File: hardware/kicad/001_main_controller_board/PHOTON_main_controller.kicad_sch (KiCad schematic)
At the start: 88 parts, among them J1 FH34SRJ-18S-0.5SH(50), J102 JST_SH RS-485_1, J103 JST_SH RS-485_2, J3 USB_C_Receptacle_USB2.0, J4 Micro_SD_Card, J6 Conn_01x04, SW1 SW_Push, U1 RP2350_60QFN, U101 APS6404L-3SQR-ZR, U102 THVD1424RGTR, U2 NCP1117-3.3_SOT223, U3 W25Q128JVPIQ, U4 TPD4E05U06DQAR, Y1 ABM8-272-T3

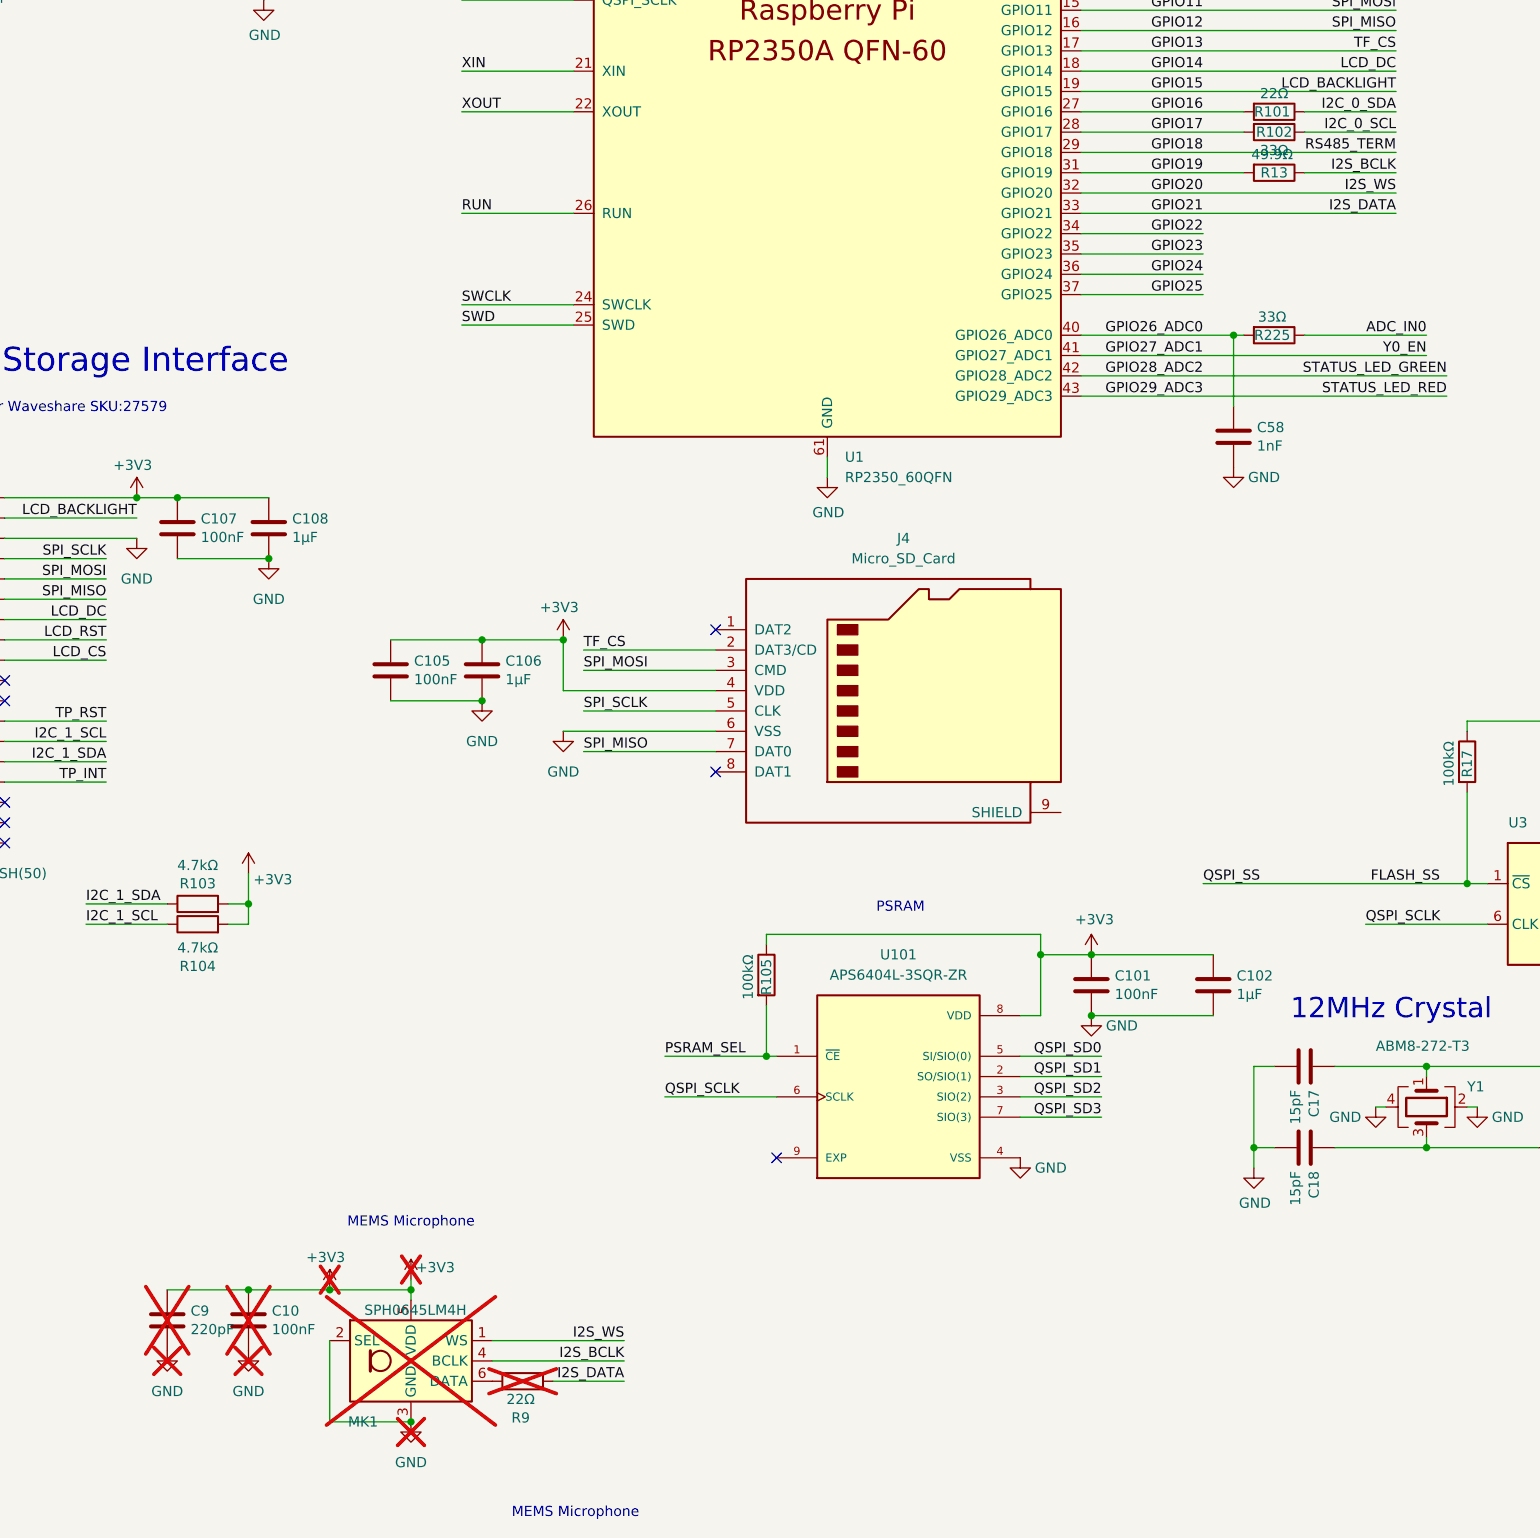
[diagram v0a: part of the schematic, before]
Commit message: Repo hygiene: untrack fab zips and committed .pyc artifacts
The production/*.zip archives are regenerable from the KiCad source, and
the BOM/positions/designators CSVs beside them stay tracked. The .pyc
files predate the __pycache__ ignore rule, so the rule never applied to
them.

Also removes production_rev B.zip, a Finder-created archive carrying
__MACOSX resource forks.

Co-Authored-By: Claude Opus 5 <noreply@anthropic.com>
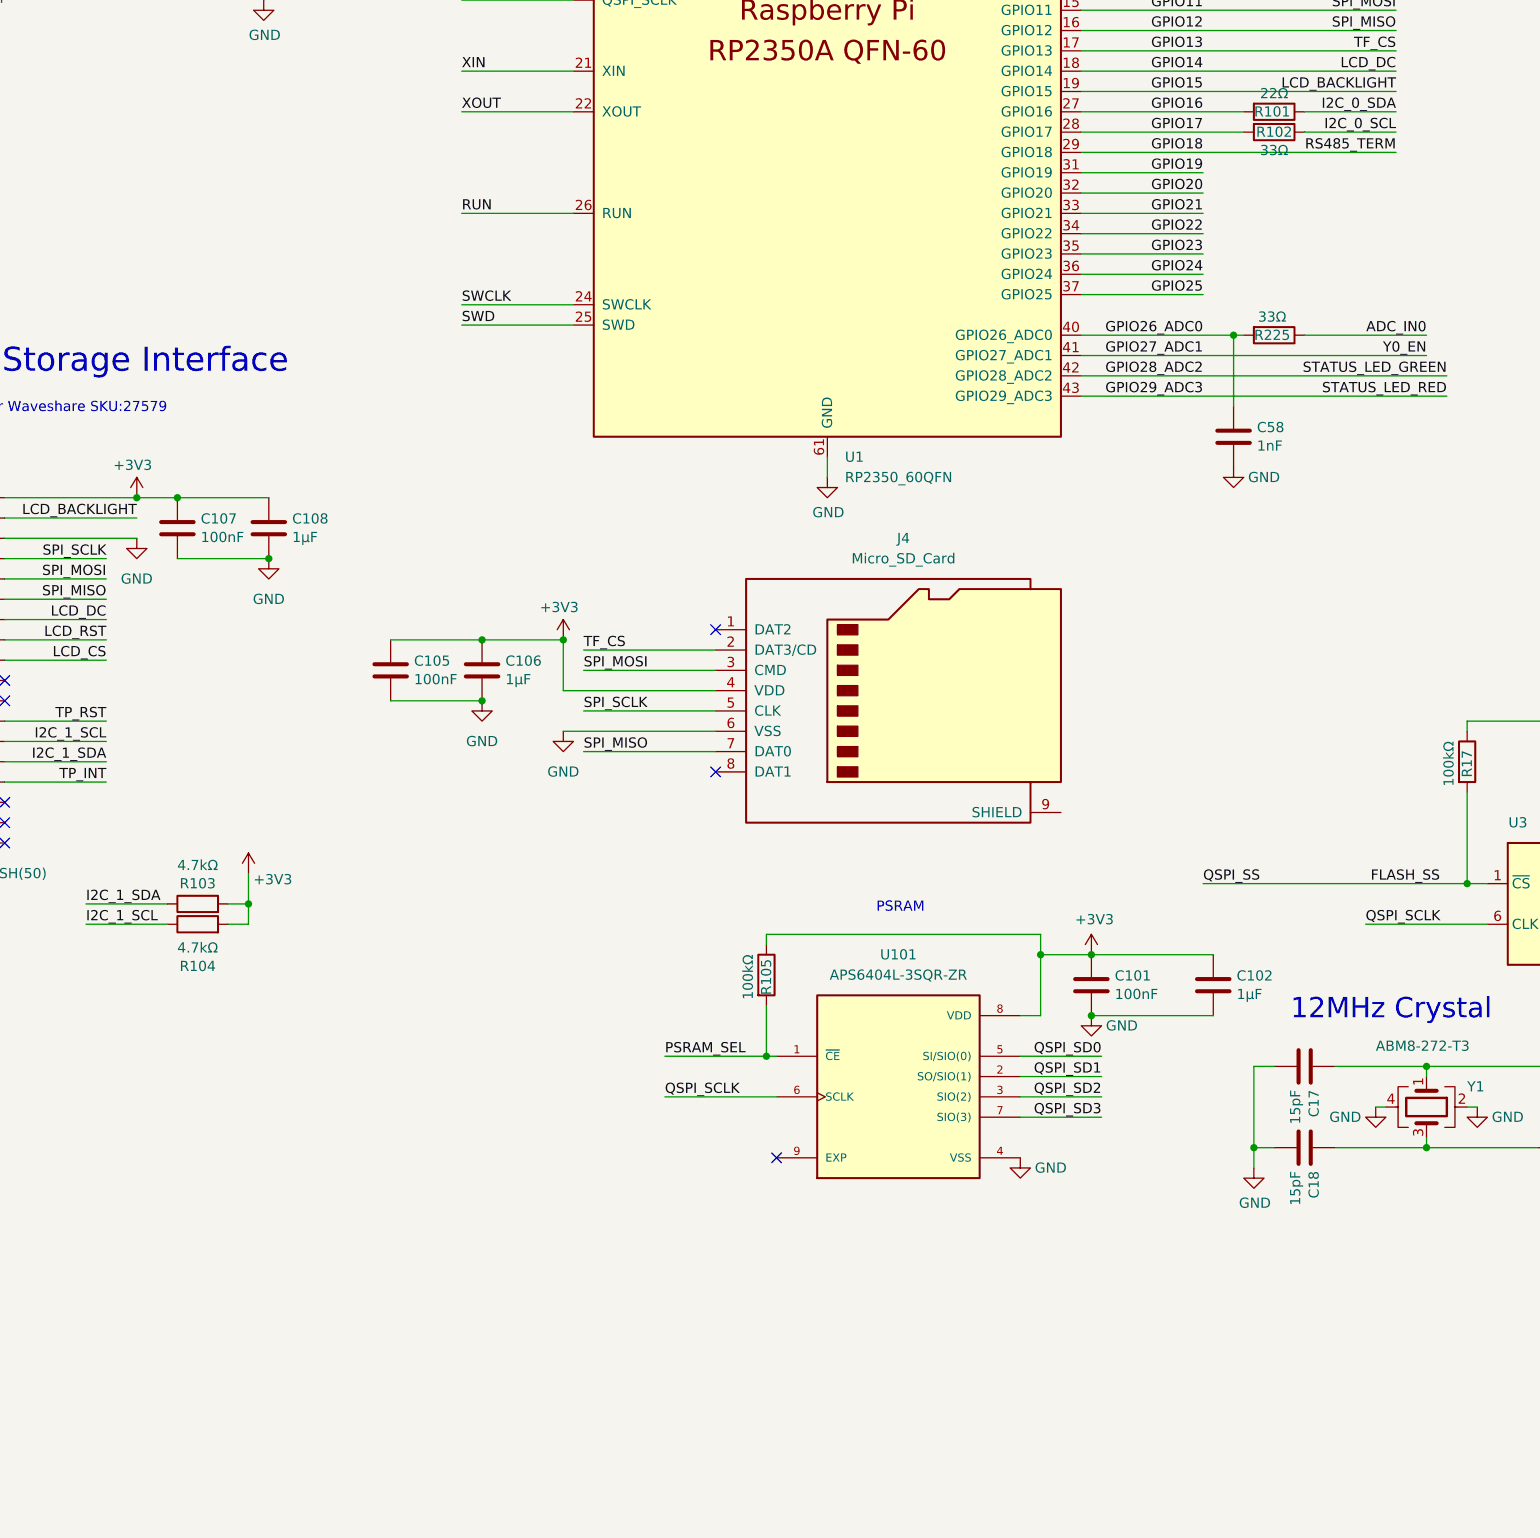
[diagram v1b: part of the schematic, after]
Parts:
- removed C10: 100nF, Capacitor_SMD:C_0402_1005Metric, symbol Device:C
- removed C9: 220pF, Capacitor_SMD:C_0402_1005Metric, symbol Device:C
- removed MK1: SPH0645LM4H, Sensor_Audio:Knowles_SPH0645LM4H-6_3.5x2.65mm, symbol Sensor_Audio:SPH0645LM4H
- removed R13: 49.9Ω, Resistor_SMD:R_0402_1005Metric, symbol Device:R
- removed R9: 22Ω, Resistor_SMD:R_0402_1005Metric, symbol Device:R
- J2: value ~ -> (none)
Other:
- note removed: "MEMS Microphone"

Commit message: Consolidate footprints into a single shared library
All three boards carried their own copies of the same footprints - 79
files across 11 project libraries for 37 distinct footprints. Several
existed three times over (RP2350-QFN-60 ThermalVias, edge_holes,
TO-236_VIS-L, SON_NT2020_VIS, L_pol_2016, USB_Micro-B). Three copies
drift, and this project has already been bitten twice by a library and
a board disagreeing.

- New hardware/kicad/common.pretty holds all 37, verified byte-identical
  where they were duplicated: zero name collisions with differing
  content, so nothing had to be reconciled.
- Each board's fp-lib-table is now a single "common" entry. Previously
  001 alone had eight, and the nickname "footprints" meant a different
  library on each of the three boards - so lib_ids were rewritten per
  board, not globally.
- 459 footprint references across the three boards now resolve. That
  includes SparkFun-Qwiic:qwiic_8mm on 001, which was referenced but
  had never been in any fp-lib-table - broken before this change.

Also shrinks docs/images/reflective_sensor.png from 2816x1536 / 4.43 MB
to 1600x873 / 1.72 MB.

Co-Authored-By: Claude Opus 5 <noreply@anthropic.com>
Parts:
- C2, C3: footprint RP2350_60QFN_minimal:C_0402_1005Metric_small_pads -> common:C_0402_1005Metric_small_pads
- J1: footprint Pretty Custom:CONN18x1_FH34SRJ-18S-0.5SH50_HIR -> common:CONN18x1_FH34SRJ-18S-0.5SH50_HIR
- J4: footprint Pretty Custom:TF-015_corrected -> common:TF-015_corrected
- L1: footprint RP2350_60QFN_minimal:L_pol_2016 -> common:L_pol_2016
- U1: footprint RP2350_60QFN_minimal:RP2350-QFN-60-1EP_7x7_P0.4mm_EP3.4x3.4mm_ThermalVias -> common:RP2350-QFN-60-1EP_7x7_P0.4mm_EP3.4x3.4mm_ThermalVias
- U101: footprint Pretty Custom:PSON50P200X300X50-9N -> common:PSON50P200X300X50-9N
- U102: footprint Pretty Custom:QFN_24RGTR_TEX -> common:QFN_24RGTR_TEX
- U3: footprint small_flash:WSON_128JVPIQ_WIN -> common:WSON_128JVPIQ_WIN
- U4: footprint Pretty Custom:DQA0010A -> common:DQA0010A
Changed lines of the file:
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@@
 			)
 		)
-		(property "Footprint" "Pretty Custom:PSON50P200X300X50-9N"
+		(property "Footprint" "common:PSON50P200X300X50-9N"
 			(at 289.56 232.41 0)
 			(hide yes)
@@
 			)
 		)
-		(property "Footprint" "Pretty Custom:CONN18x1_FH34SRJ-18S-0.5SH50_HIR"
+		(property "Footprint" "common:CONN18x1_FH34SRJ-18S-0.5SH50_HIR"
 			(at 172.72 180.34 0)
 			(hide yes)
@@
 			)
 		)
-		(property "Footprint" "Pretty Custom:TF-015_corrected"
+		(property "Footprint" "common:TF-015_corrected"
 			(at 318.77 176.53 0)
 			(hide yes)
@@
 			)
 		)
-		(property "Footprint" "RP2350_60QFN_minimal:C_0402_1005Metric_small_pads"
+		(property "Footprint" "common:C_0402_1005Metric_small_pads"
 			(at 191.4652 71.12 0)
 			(hide yes)
@@
 			)
 		)
-		(property "Footprint" "small_flash:WSON_128JVPIQ_WIN"
+		(property "Footprint" "common:WSON_128JVPIQ_WIN"
 			(at 375.92 210.82 0)
 			(hide yes)
@@
 			)
 		)
-		(property "Footprint" "RP2350_60QFN_minimal:RP2350-QFN-60-1EP_7x7_P0.4mm_EP3.4x3.4mm_ThermalVias"
+		(property "Footprint" "common:RP2350-QFN-60-1EP_7x7_P0.4mm_EP3.4x3.4mm_ThermalVias"
 			(at 261.62 104.14 0)
 			(hide yes)
@@
 			)
 		)
-		(property "Footprint" "RP2350_60QFN_minimal:L_pol_2016"
+		(property "Footprint" "common:L_pol_2016"
 			(at 217.17 67.31 0)
 			(hide yes)
@@
 			)
 		)
-		(property "Footprint" "Pretty Custom:DQA0010A"
+		(property "Footprint" "common:DQA0010A"
 			(at 66.04 266.7 0)
 			(hide yes)
@@
 			)
 		)
-		(property "Footprint" "Pretty Custom:QFN_24RGTR_TEX"
+		(property "Footprint" "common:QFN_24RGTR_TEX"
 			(at 100.33 160.02 0)
 			(hide yes)
@@
 			)
 		)
-		(property "Footprint" "RP2350_60QFN_minimal:C_0402_1005Metric_small_pads"
+		(property "Footprint" "common:C_0402_1005Metric_small_pads"
 			(at 202.8952 71.12 0)
 			(hide yes)

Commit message: Rename shared footprint library common -> photon_common
'common' is too generic for a library nickname - it can collide with a
global library or another project's table, and it doesn't identify whose
footprints these are.

155 lib_ids rewritten across the three boards plus all three
fp-lib-tables. All 459 footprint references still resolve.

Co-Authored-By: Claude Opus 5 <noreply@anthropic.com>
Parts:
- C2, C3: footprint common:C_0402_1005Metric_small_pads -> photon_common:C_0402_1005Metric_small_pads
- J1: footprint common:CONN18x1_FH34SRJ-18S-0.5SH50_HIR -> photon_common:CONN18x1_FH34SRJ-18S-0.5SH50_HIR
- J4: footprint common:TF-015_corrected -> photon_common:TF-015_corrected
- L1: footprint common:L_pol_2016 -> photon_common:L_pol_2016
- U1: footprint common:RP2350-QFN-60-1EP_7x7_P0.4mm_EP3.4x3.4mm_ThermalVias -> photon_common:RP2350-QFN-60-1EP_7x7_P0.4mm_EP3.4x3.4mm_ThermalVias
- U101: footprint common:PSON50P200X300X50-9N -> photon_common:PSON50P200X300X50-9N
- U102: footprint common:QFN_24RGTR_TEX -> photon_common:QFN_24RGTR_TEX
- U3: footprint common:WSON_128JVPIQ_WIN -> photon_common:WSON_128JVPIQ_WIN
- U4: footprint common:DQA0010A -> photon_common:DQA0010A
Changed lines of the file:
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@@
 			)
 		)
-		(property "Footprint" "common:PSON50P200X300X50-9N"
+		(property "Footprint" "photon_common:PSON50P200X300X50-9N"
 			(at 289.56 232.41 0)
 			(hide yes)
@@
 			)
 		)
-		(property "Footprint" "common:CONN18x1_FH34SRJ-18S-0.5SH50_HIR"
+		(property "Footprint" "photon_common:CONN18x1_FH34SRJ-18S-0.5SH50_HIR"
 			(at 172.72 180.34 0)
 			(hide yes)
@@
 			)
 		)
-		(property "Footprint" "common:TF-015_corrected"
+		(property "Footprint" "photon_common:TF-015_corrected"
 			(at 318.77 176.53 0)
 			(hide yes)
@@
 			)
 		)
-		(property "Footprint" "common:C_0402_1005Metric_small_pads"
+		(property "Footprint" "photon_common:C_0402_1005Metric_small_pads"
 			(at 191.4652 71.12 0)
 			(hide yes)
@@
 			)
 		)
-		(property "Footprint" "common:WSON_128JVPIQ_WIN"
+		(property "Footprint" "photon_common:WSON_128JVPIQ_WIN"
 			(at 375.92 210.82 0)
 			(hide yes)
@@
 			)
 		)
-		(property "Footprint" "common:RP2350-QFN-60-1EP_7x7_P0.4mm_EP3.4x3.4mm_ThermalVias"
+		(property "Footprint" "photon_common:RP2350-QFN-60-1EP_7x7_P0.4mm_EP3.4x3.4mm_ThermalVias"
 			(at 261.62 104.14 0)
 			(hide yes)
@@
 			)
 		)
-		(property "Footprint" "common:L_pol_2016"
+		(property "Footprint" "photon_common:L_pol_2016"
 			(at 217.17 67.31 0)
 			(hide yes)
@@
 			)
 		)
-		(property "Footprint" "common:DQA0010A"
+		(property "Footprint" "photon_common:DQA0010A"
 			(at 66.04 266.7 0)
 			(hide yes)
@@
 			)
 		)
-		(property "Footprint" "common:QFN_24RGTR_TEX"
+		(property "Footprint" "photon_common:QFN_24RGTR_TEX"
 			(at 100.33 160.02 0)
 			(hide yes)
@@
 			)
 		)
-		(property "Footprint" "common:C_0402_1005Metric_small_pads"
+		(property "Footprint" "photon_common:C_0402_1005Metric_small_pads"
 			(at 202.8952 71.12 0)
 			(hide yes)
